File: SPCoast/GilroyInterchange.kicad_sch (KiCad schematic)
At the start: 72 parts, among them SW5777 777, SW5781 781

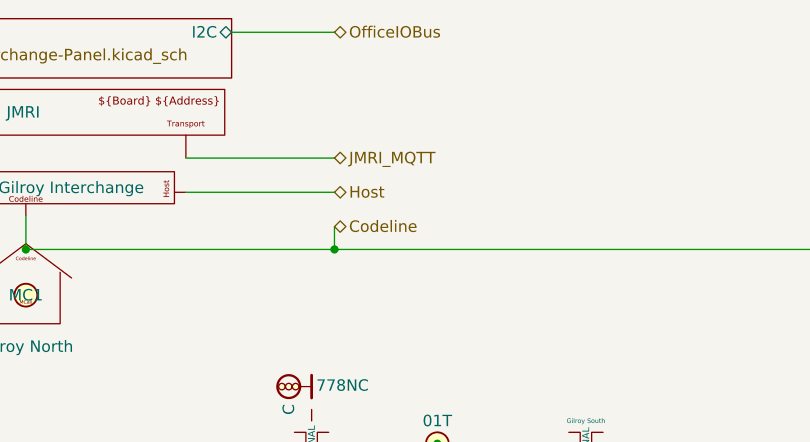
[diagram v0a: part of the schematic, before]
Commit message: fix(kicad): port names match across sheet boundaries: OfficeIOBus and IOBus
SPCoast/edits/2026-10-21-port-names.py: the Luchessa sheet box's pin OfficeBusIO -> OfficeIOBus;
Gilroy Interchange's attachment label JMRI_MQTT -> IOBus.

Verified: netlist before/after: Luchessa's three MAX7313s rejoin the desk bus net with JohnCTC
and the two Gilroy panels; RIO2 is on the JMRI_MQTT transport; every other net unchanged.
ERC: no label mismatches or isolated labels remain; what is left is unwired bus pins.

Co-Authored-By: Claude Fable 5.1 <noreply@anthropic.com>
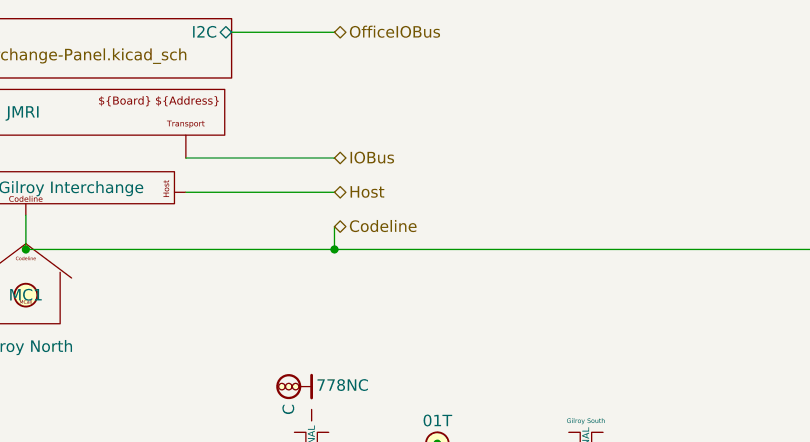
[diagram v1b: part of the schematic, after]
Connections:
- net JMRI_MQTT renamed IOBus
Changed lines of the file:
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@@
 		)
 	)
-	(hierarchical_label "JMRI_MQTT"
+	(hierarchical_label "IOBus"
 		(shape bidirectional)
 		(at 109.22 29.21 0)
